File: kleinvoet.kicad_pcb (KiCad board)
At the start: 4 copper layers, 60 x 123 mm, 190 parts, among them J1 Conn_ST_STDC14, J11 Micro_SD_Card_Det, J12 JST-PH, J13 USB_C_Receptacle_USB2.0, J16 GPS_Transmission_Conn, J2 FTDI_Conn, J3 Sensor_Conn, J4 GPS_Transmission_Conn, J6 Sensor_Conn, Q1 PMOS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

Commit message: Route ST-Link
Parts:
- J4: moved to B.Cu
- moved C2 10.1 mm to (122.0, 78.2)
- moved J4 3.94 mm to (125.5, 106.2)
- moved R1 3.48 mm to (120.8, 68.8), turned to 270 degrees
- moved TP9 0.05 mm to (131.0, 54.2)
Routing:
- net /SWDIO: track 0.00 -> 22.9 mm
- net /SWCLK: track 0.00 -> 19.6 mm
- net /D3: track 0.00 -> 17.2 mm
- net Net-(R1-Pad1): track 0.00 -> 8.24 mm
- net /SDIO_CMD: track 30.1 -> 33.1 mm
- net /ADC_SAI_SD_B: track 31.2 -> 33.6 mm
- net +3.3VADC: track 26.1 -> 27.9 mm
- net /SDIO_CLK: track 34.7 -> 36.4 mm
- net +3V3: track 44.2 -> 42.9 mm
- net GND: track 149.4 -> 148.6 mm, vias 372 -> 371
- net /SDIO_D1: track 42.5 -> 43.2 mm
- net /SDIO_D0: track 41.8 -> 42.4 mm

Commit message: (WIP) SD config
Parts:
- moved TP11 13.7 mm to (135.8, 35.2)
- moved TP10 12.1 mm to (135.8, 36.8)
- moved TP7 11.5 mm to (135.8, 38.2)
- moved TP8 10.8 mm to (142.9, 39.5)
- moved R65 5.55 mm to (113.4, 80.5)
- moved C2 4.79 mm to (120.2, 73.8)
- moved C3 4.46 mm to (110.0, 81.6)
- moved JP8 4.44 mm to (113.4, 82.8)
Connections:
- J11 pad 10: /D7 -> /A5
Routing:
- net /A5: track 0.00 -> 25.8 mm, vias 0 -> 1
- net GND: track 148.6 -> 158.4 mm, vias 371 -> 381
- net Net-(J11-Pad9): track 0.00 -> 8.76 mm, vias 0 -> 1
- net Net-(JP8-Pad2): track 0.00 -> 2.63 mm
- net /A4: track 37.4 -> 39.3 mm
- net /ADC_CTRL_SCL: track 38.5 -> 40.1 mm
- net /ADC_SAI_FS: track 35.8 -> 37.3 mm
- net /ADC_CTRL_SDA: track 37.1 -> 38.6 mm
- net +3V3: track 42.9 -> 42.8 mm, vias 35 -> 46

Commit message: Route Misc.
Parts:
- moved R88 66.2 mm to (106.3, 72.4), turned to 0 degrees
- moved D7 66.0 mm to (106.4, 74.3), turned to 0 degrees
- moved R7 53.4 mm to (120.5, 82.3), turned to 270 degrees
- moved D8 48.4 mm to (117.0, 82.3), turned to 270 degrees
- moved R6 46.9 mm to (122.2, 82.4), turned to 270 degrees
- moved D9 46.0 mm to (118.8, 82.3), turned to 270 degrees
- moved D1 35.3 mm to (144.3, 80.2)
- moved R8 34.9 mm to (138.4, 80.2), turned to 90 degrees
- moved R2 34.9 mm to (142.3, 80.2)
- moved D10 29.6 mm to (140.4, 80.3), turned to 270 degrees
- moved R89 14.0 mm to (106.3, 68.6), turned to 0 degrees
- moved CB9 4.06 mm to (106.3, 70.5), turned to 0 degrees
- moved FB9 2.03 mm to (140.8, 69.8), turned to 90 degrees
- moved CB1 1.92 mm to (106.3, 76.2), turned to 0 degrees
- moved CB4 0.25 mm to (140.0, 65.9)
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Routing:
- net /D0: track 0.00 -> 38.9 mm, vias 0 -> 2
- net /D1: track 0.00 -> 33.9 mm, vias 0 -> 2
- net Earth: track 87.9 -> 120.1 mm
- net GND: track 158.4 -> 186.5 mm, vias 381 -> 401
- net +3V3: track 42.8 -> 65.3 mm, vias 46 -> 68
- net /~RST: track 44.3 -> 66.2 mm, vias 1 -> 3
- net /D15: track 0.00 -> 8.66 mm
- net /GNSS_Module/GPS_SYNC: track 6.68 -> 0.00 mm
- net Net-(D8-Pad2): track 0.00 -> 6.00 mm
- net /SDIO_D3: track 29.6 -> 33.6 mm, vias 1 -> 2
- net Net-(D7-Pad2): track 0.00 -> 1.92 mm
- net Net-(D9-Pad2): track 0.00 -> 1.77 mm

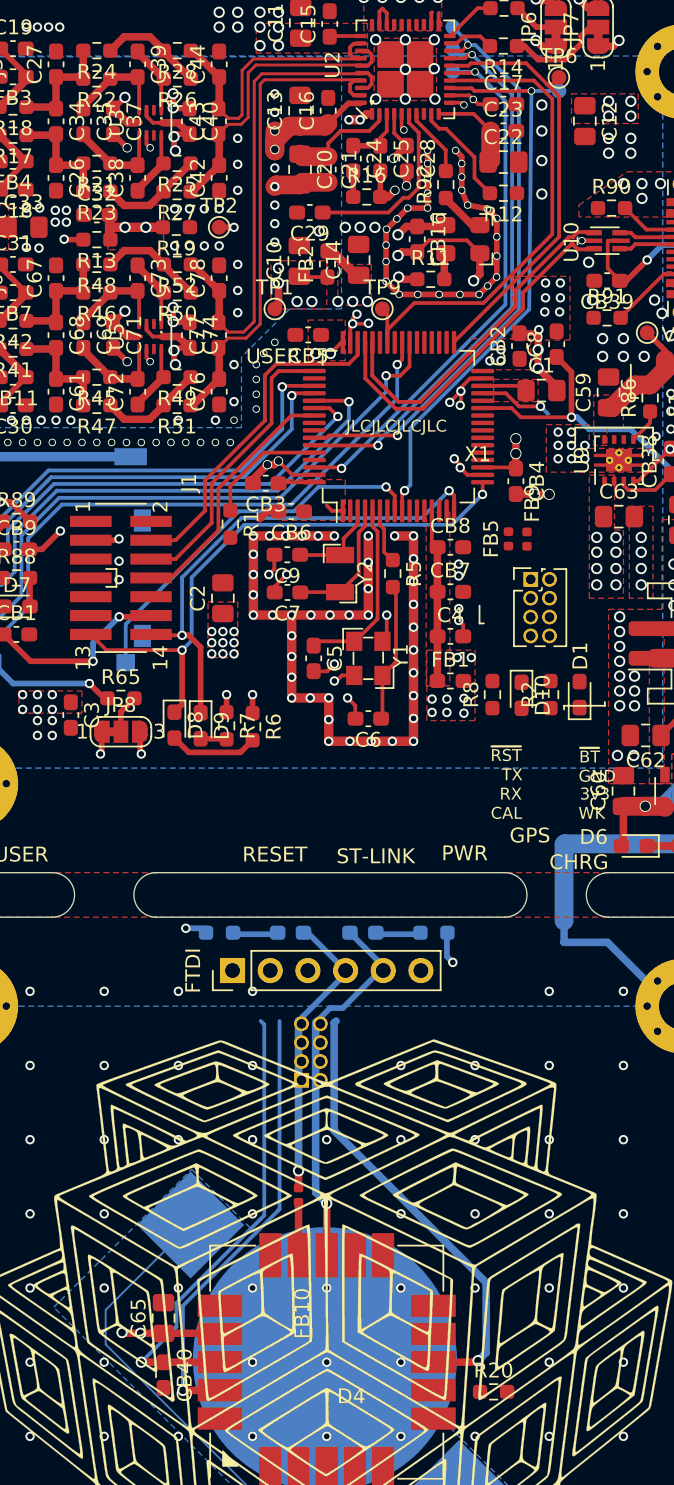
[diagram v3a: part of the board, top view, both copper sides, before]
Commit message: Route GPS Conn
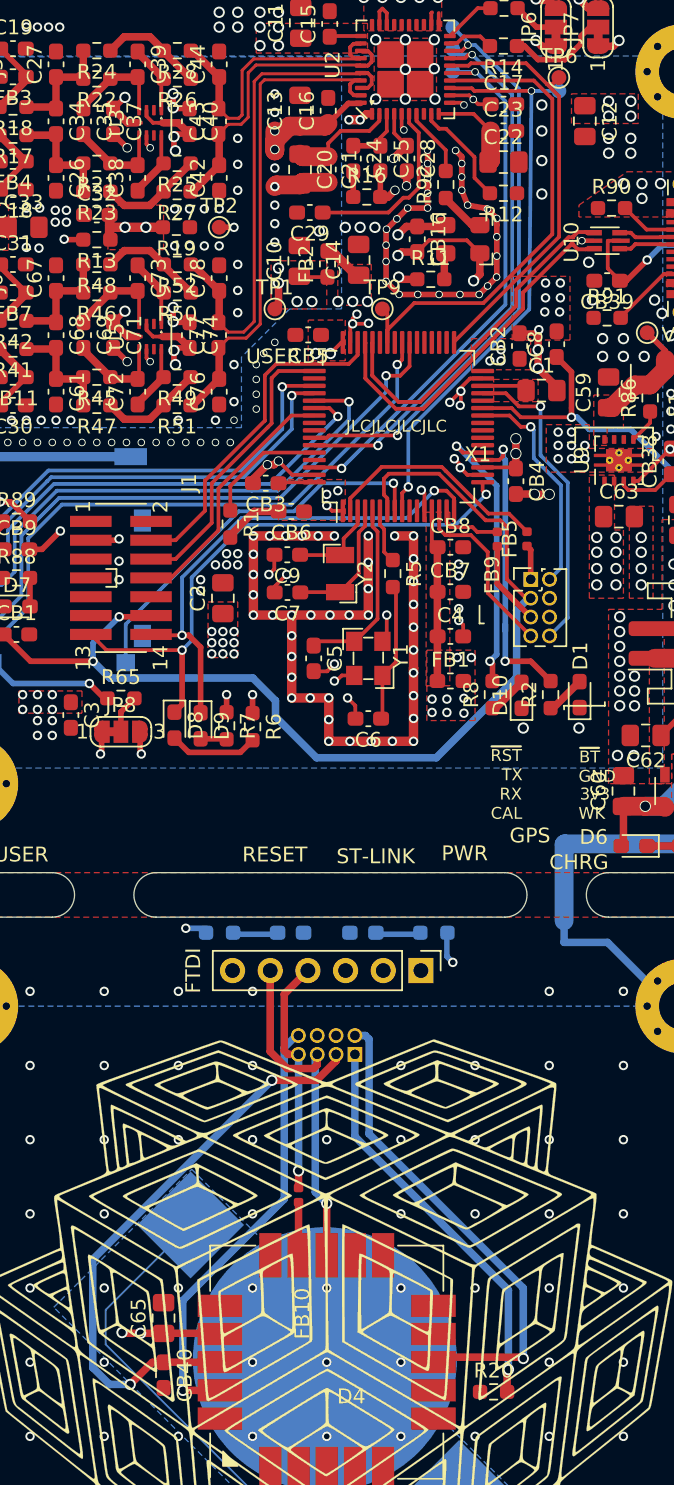
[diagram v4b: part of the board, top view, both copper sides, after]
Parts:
- moved J2 12.7 mm to (133.6, 98.8), turned to 270 degrees
- moved J4 4.00 mm to (129.2, 104.5), turned to 90 degrees
- moved FB9 2.00 mm to (138.8, 69.8), turned to 270 degrees
- moved FB5 1.25 mm to (140.8, 69.8)
- turned D10 to 90 degrees
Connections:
- J16 pad 1: /~RST -> /GNSS_Module/GPS_SYNC
- J16 pad 3: /A0 -> /~RST
- J16 pad 7: /GNSS_Module/GPS_SYNC -> /A0
- J4 pad 1: /~RST -> /GNSS_Module/GPS_SYNC
- J4 pad 3: /A0 -> /~RST
- J4 pad 7: /GNSS_Module/GPS_SYNC -> /A0
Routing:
- net /~RST: track 66.2 -> 131.5 mm, vias 3 -> 4
- net /GNSS_Module/GPS_SYNC: track 0.00 -> 29.4 mm, vias 0 -> 1
- net /A2: track 0.00 -> 20.4 mm, vias 0 -> 2
- net /D13: track 0.00 -> 19.2 mm, vias 0 -> 2
- net /A3: track 30.5 -> 48.1 mm, vias 1 -> 2
- net /D6: track 35.1 -> 50.7 mm
- net /RTC_CAL: track 0.00 -> 15.4 mm
- net /A0: track 20.6 -> 28.1 mm
- net /A1: track 0.00 -> 4.50 mm
- net GND: track 186.5 -> 190.6 mm, vias 401 -> 411
- net /GNSS_Module/GPS_RX: track 25.5 -> 29.5 mm
- net Net-(D1-Pad2): track 0.00 -> 2.70 mm
- net Net-(D10-Pad2): track 0.00 -> 2.68 mm
- net /A5: track 25.8 -> 26.5 mm
- net +3V3: vias 68 -> 71

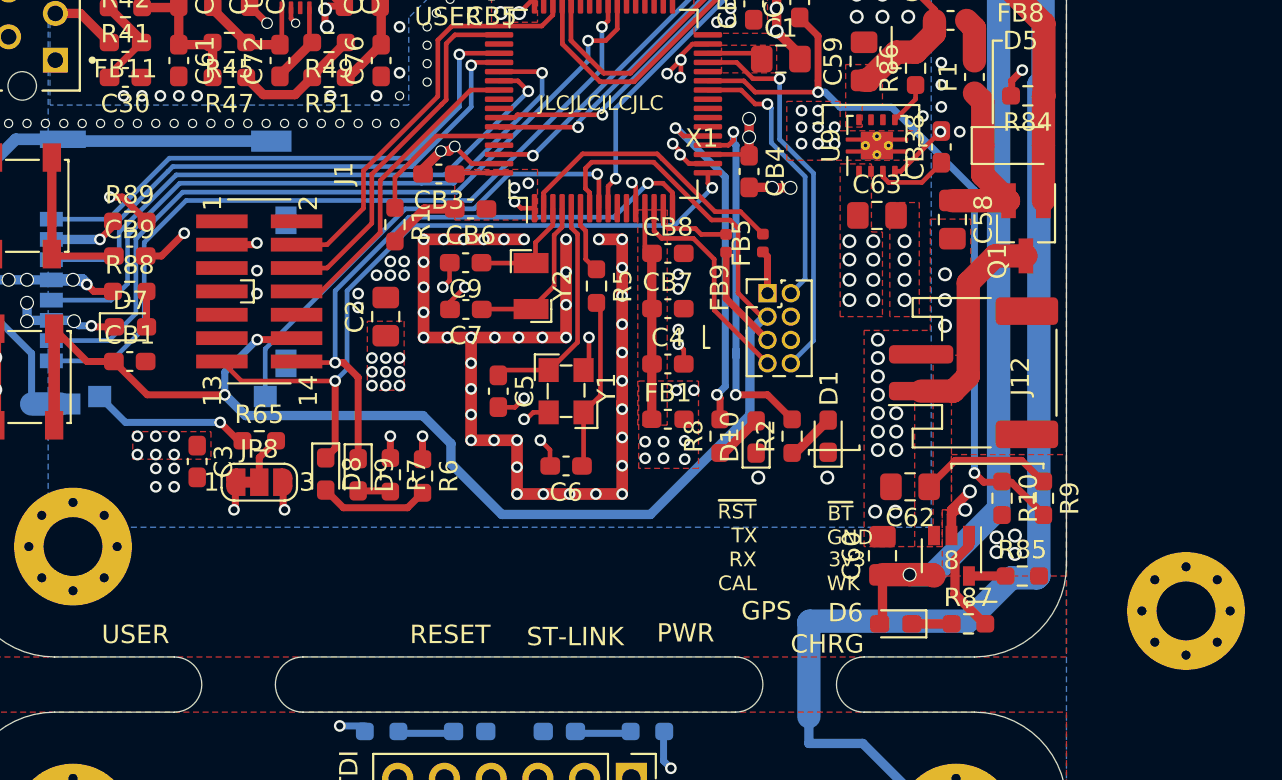
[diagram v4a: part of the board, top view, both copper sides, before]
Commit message: Route USR BTN
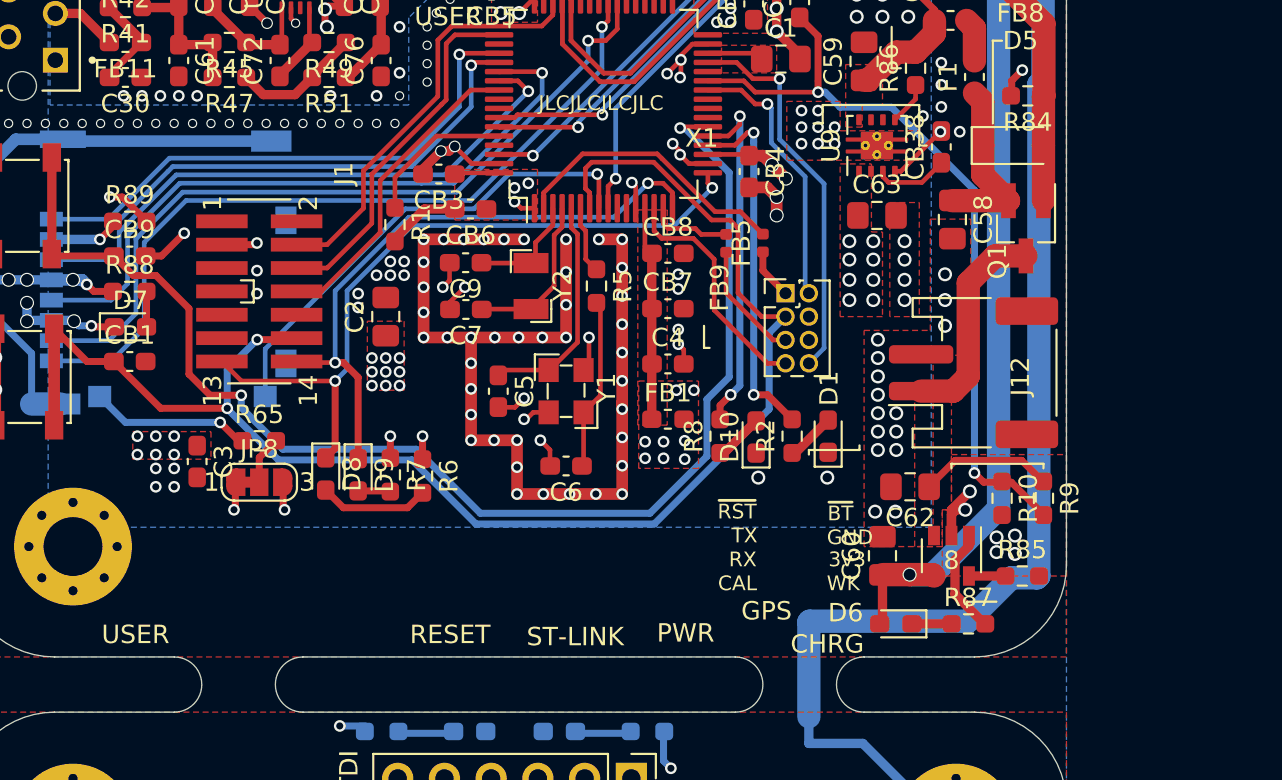
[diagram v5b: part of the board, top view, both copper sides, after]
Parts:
- removed H4: MountingHole_Pad, MountingHole:MountingHole_3.2mm_M3_Pad_Via
- moved J16 0.98 mm to (142.0, 72.5)
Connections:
- CB9 pad 1: /D15 -> /D12
- SW2 pad 1: /D15 -> /D12
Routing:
- net /D12: track 0.00 -> 71.6 mm, vias 0 -> 2
- net /D15: track 8.66 -> 0.00 mm
- net /~RST: track 131.5 -> 133.7 mm
- net /A0: track 28.1 -> 29.1 mm
- net /GNSS_Module/GPS_RX: track 29.5 -> 30.3 mm
- net /A2: track 20.4 -> 19.7 mm
- net +3V3: track 65.3 -> 65.8 mm

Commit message: Fix GPS conn.
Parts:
- moved R3 14.6 mm to (120.8, 101.2), turned to 0 degrees
- moved R4 14.6 mm to (133.8, 101.2), turned to 180 degrees
- moved D3 6.78 mm to (129.4, 101.2), turned to 0 degrees
- moved D2 6.78 mm to (125.1, 101.2), turned to 180 degrees
- moved J2 0.85 mm to (133.6, 98.0)
- moved J4 0.75 mm to (129.2, 105.2)
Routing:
- net GND: track 191.0 -> 197.1 mm
- net /A0: track 29.1 -> 34.3 mm
- net /GNSS_Module/GPS_RX: track 30.3 -> 35.2 mm
- net +3V3: track 65.8 -> 64.8 mm
- net /A3: track 47.9 -> 47.0 mm
- net /D6: track 50.8 -> 50.1 mm
- net /GNSS_Module/GPS_SYNC: track 29.8 -> 29.1 mm
- net /A5: track 26.5 -> 27.2 mm
- net Net-(D2-Pad2): track 3.04 -> 2.52 mm
- net Net-(D3-Pad2): track 3.04 -> 2.52 mm
